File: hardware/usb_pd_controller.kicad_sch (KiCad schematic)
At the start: 87 parts, among them J4 SolderWire-1.5sqmm, J5 Banana_4mm_Red, J6 Banana_4mm_Black, Q1 BSS138, Q2 BSS138, Q3 SQJB60EP, Q5 SQJB60EP, U1 AP33772SDKZ-13-FA02, U11 TPS55340PWPR, U12 LM74801-Q1, U13 74LVC1G08, U3 INA226, U5 AOZ1284PI, U6 TL431AIDBZR

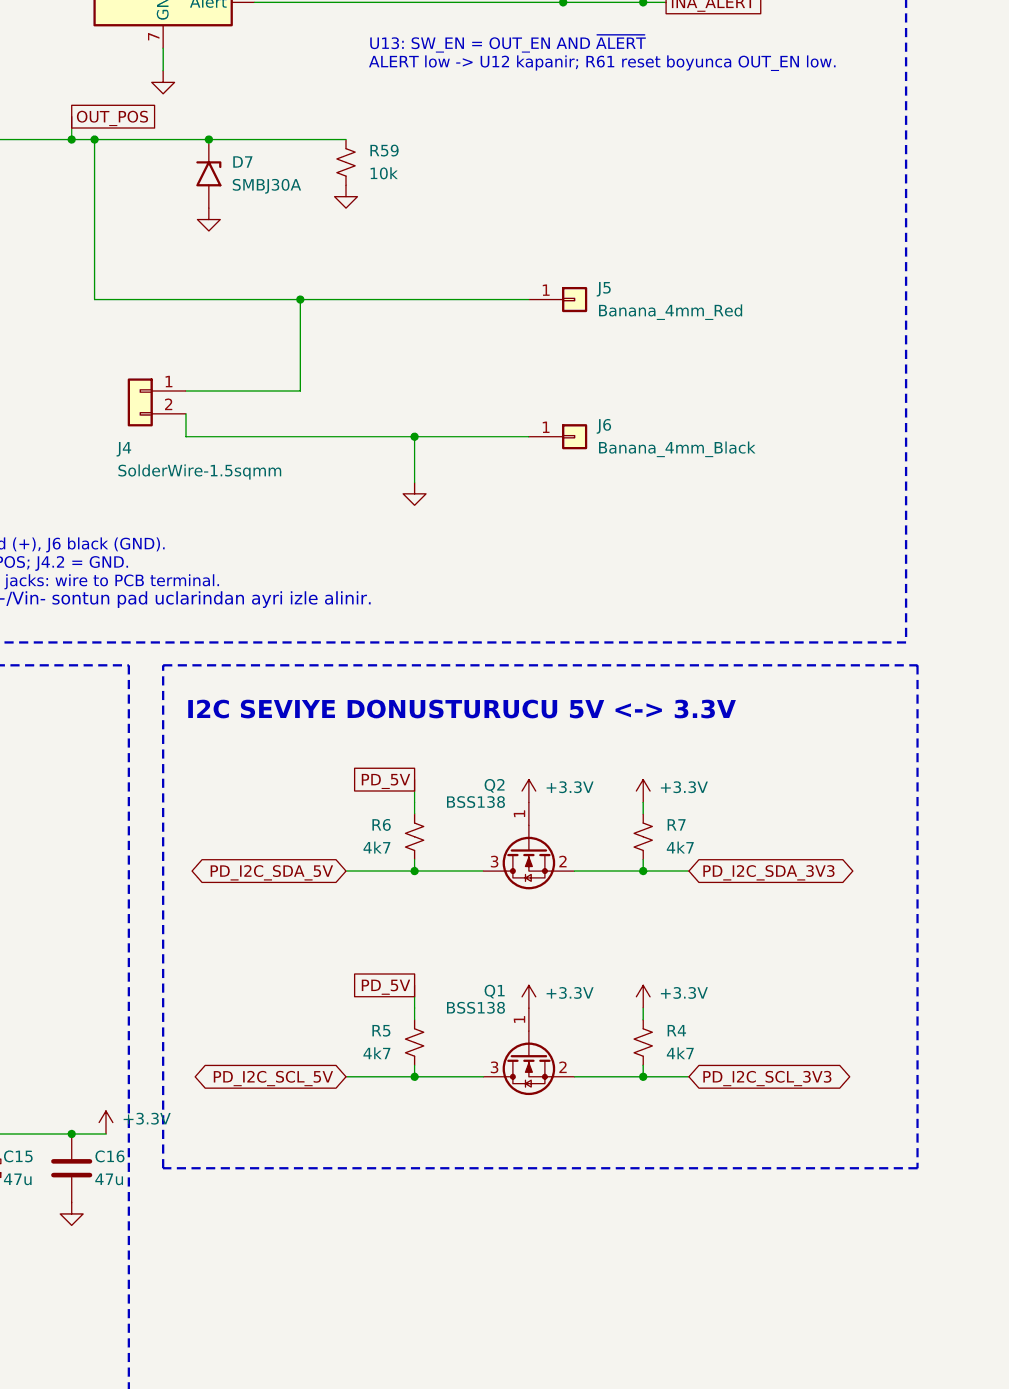
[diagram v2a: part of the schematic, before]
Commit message: hardware: I2C seviye dönüştürücüyü mcu'ya taşı, OUT_POS aktif deşarjı ekle (TASK-048/049/050)
- mcu: I2C seviye dönüştürücü (Q1, Q2, R4-R7) usb_pd_controller'dan
  taşındı; sayfa A4 -> A3. Bağlantı değişmedi.
- usb_pd_controller: R59 bleed yerine SW_EN kontrollü deşarj. Q4 BSS138P
  SW_EN'i ters çevirir, Q6 BSS138P OUT_POS'u R67 1k 2W 2512 üzerinden
  boşaltır; gate SW_OUT'tan R66 100k, D10 BZT52C12 ile 12 V. R59 10k 0805
  -> 100k 0603. Q1/Q2 alanları BSS138P,215 datasheet'ine göre düzeltildi.
- Karar: design_decisions/output/CIKIS_DESARJI_20260923.md; firmware
  deşarj bekleme ve dış kaynak uyarısı FIRMWARE_GEREKSINIMLERI.md §3.
- Backlog: TASK-048/049 Done, TASK-050 bring-up doğrulaması açıldı,
  TASK-006'ya footprint notu.

Kanıt: ERC 0/0. Netlist farkı yalnız beklenen netler: yeni DISCH_G
(D10.1, Q4.3, Q6.1, R66.2) ve Net-(Q6-D) (Q6.3, R67.2); SW_EN += Q4.1,
SW_OUT += R66.1, OUT_POS += R67.1, GND += D10.2, Q4.2, Q6.2.

Co-Authored-By: Claude Opus 5.5 <noreply@anthropic.com>
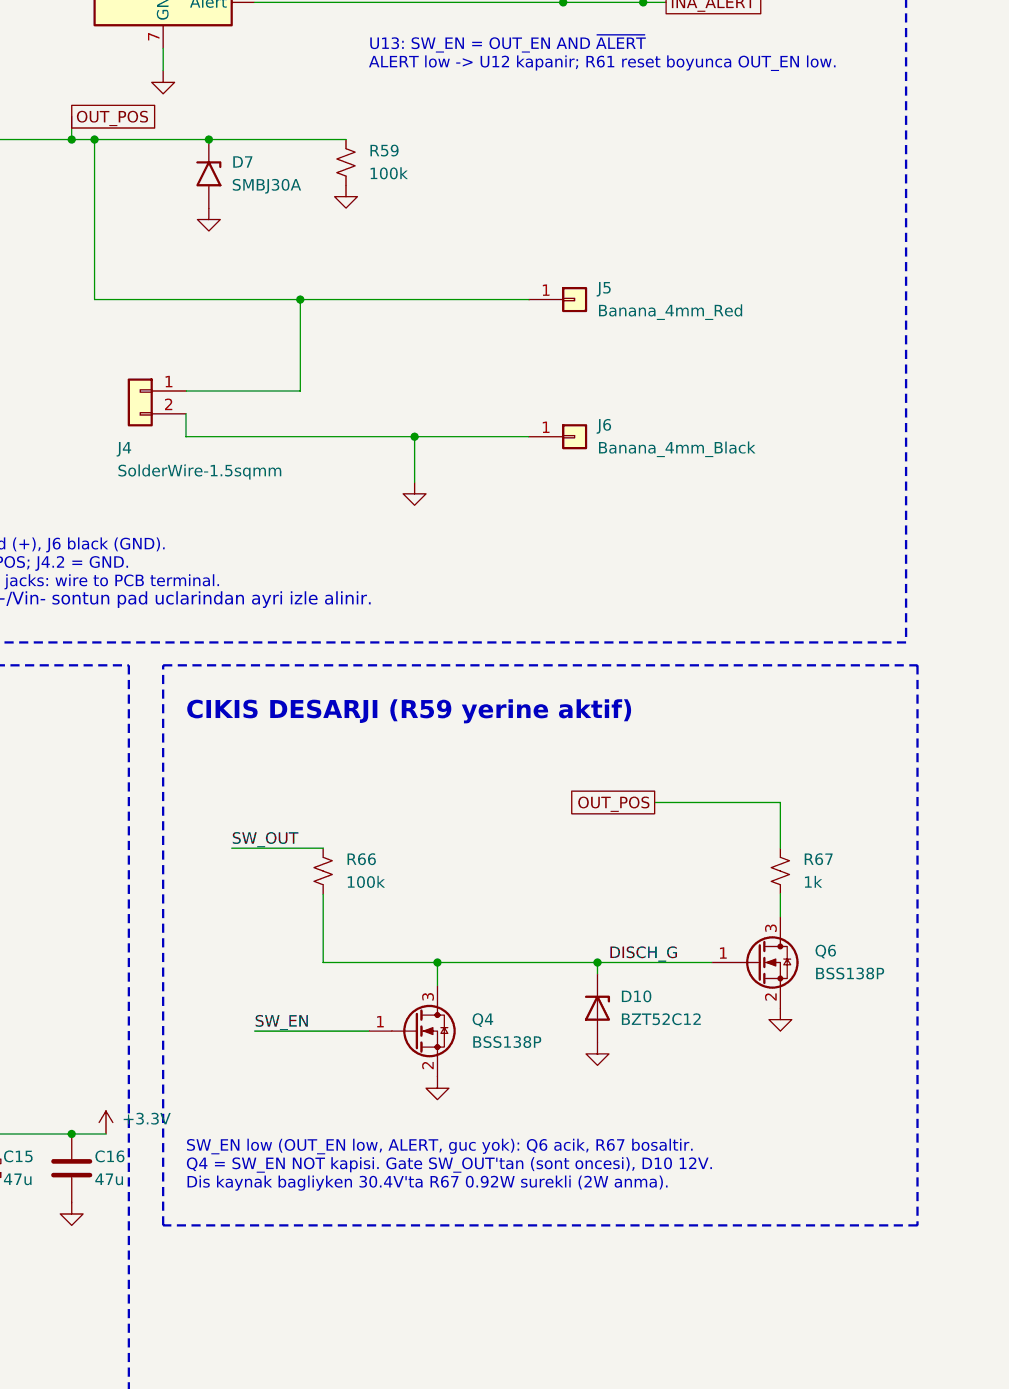
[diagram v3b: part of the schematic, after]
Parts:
- removed Q1, Q2: BSS138, Package_TO_SOT_SMD:SOT-23, symbol Transistor_FET:BSS138
- removed R4, R5, R6, R7: 4k7, Resistor_SMD:R_0402_1005Metric, symbol Device:R_Small_US
- added D10: BZT52C12, Diode_SMD:D_SOD-123, symbol Device:D_Zener
- added Q4, Q6: BSS138P, Package_TO_SOT_SMD:SOT-23, symbol Transistor_FET:BSS138
- added R66: 100k, Resistor_SMD:R_0603_1608Metric, symbol Device:R_Small_US
- added R67: 1k, Resistor_SMD:R_2512_6332Metric, symbol Device:R_Small_US
- R59: value 10k -> 100k; footprint Resistor_SMD:R_0805_2012Metric -> Resistor_SMD:R_0603_1608Metric; Composition High Power Thick Film -> Thick Film; DesignNote OUT_POS bleed. 30V OVLO esiginde 90mW; %50 azaltma ile >=0.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 -> OUT_POS son bleed: Q6 eşiği (~1.5V) altını boşaltır, INA226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; MPN HP05W3F1002T5E -> CRCW0603100KFKTBBC; Manufacturer Royalohm -> Vishay; Package 0805 (2012 Metric) -> 0603 (1608 Metric); PowerRating 0.333W -> 0.1W; SelectionNote Özdisan 604238; stok 710 (21.09.2026); Uygun. 21.09 üçüncü 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 -> Özdisan 1089735; stok 8494 (23.09.2026); Uygun.; VoltageRating 150V -> 75V
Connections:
- net GND: now also D10.2 (A), Q4.2 (S), Q6.2 (S)
- net OUT_POS: now also R67.1
- net SW_EN: now also Q4.1 (G)
- net SW_OUT: now also R66.1
- new net: Q6.3 (D), R67.2
- new net DISCH_G: D10.1 (K), Q4.3 (D), Q6.1 (G), R66.2
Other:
- note added: "CIKIS DESARJI (R59 yerine aktif)"
- note added: "SW_EN low (OUT_EN low, ALERT, guc yok): Q6 acik, R67 bosaltir. Q4 = SW_EN NOT kapisi. Gate SW_OUT'tan (sont oncesi), D10 12V. Dis kaynak bagliyken 30.4V'ta R67 0.92W surekli (2W anma)."
- note removed: "I2C SEVIYE DONUSTURUCU 5V <-> 3.3V"

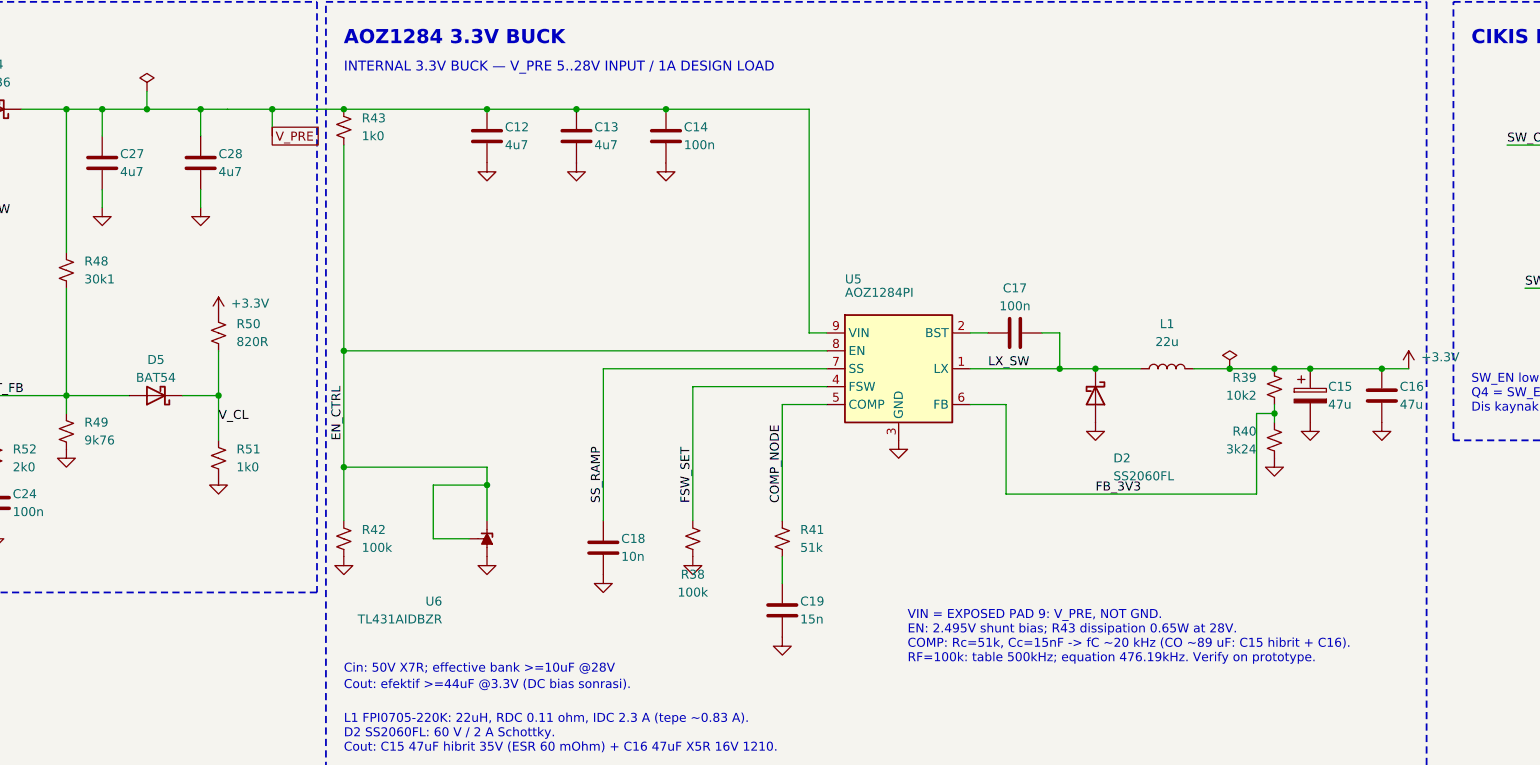
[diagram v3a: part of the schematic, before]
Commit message: hardware: U5 EN ve U11 FB clamp icin ortak V_X referansi (TASK-057)
FB clamp referansi (V_CL) +3.3V'tan besleniyordu; +3.3V ise V_PRE'den
uretildigi icin acilista ve 3V3 kaybinda clamp FB'yi asagi cekiyordu.
EN_CTRL ve clamp tek TLV431 dugumunde birlesti: V_X = 1.605 V.

- U6 TL431AIDBZR -> TLV431BQDBZT; yeni proje sembolu
  Power_Path_Custom:TLV431xDBZ (DBZ: 1=REF, 2=K, 3=A, SLVS139Z Tablo 4-1)
- R50 2k87 / R51 9k76 U6 REF bolucusu oldu, U6 yanina tasindi
- D5 BAT54 (SOD-123) -> BAS16HT1G (SOD-323), katot EN_CTRL'de
- R43 1k0 2W -> 4k7 1W (28 V'ta 0.65 W -> 0.15 W), R42 kaldirildi

Worst-case (0-60 C, V_PRE 4.3-34 V): FB <= 2.40 V (abs 3 V), EN
1.566-1.652 V, U6 akimi 0.41-7.8 mA. ERC 0/0; netlist farki yalniz
EN_CTRL, yeni Net-(U6-REF), V_CL kalkti, +3.3V/GND'den R50/R42 cikti.
PCB guncellemesi TASK-058, olcum TASK-059.

Co-Authored-By: Claude Opus 5.5 <noreply@anthropic.com>
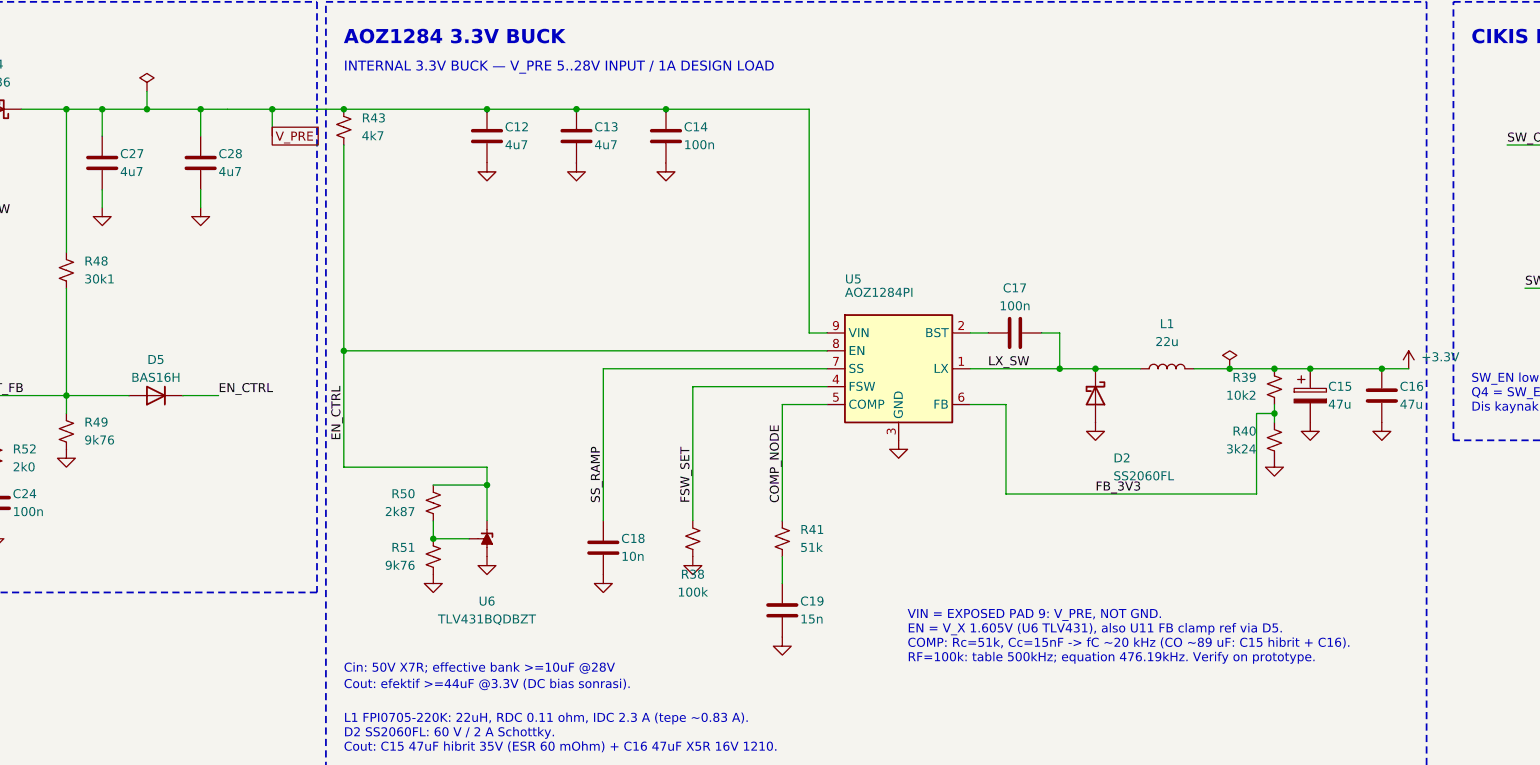
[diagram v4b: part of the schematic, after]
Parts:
- removed R42: 100k, Resistor_SMD:R_0402_1005Metric, symbol Device:R_Small_US
- D5: value BAT54 -> BAS16H; footprint Diode_SMD:D_SOD-123 -> Diode_SMD:D_SOD-323; symbol Device:D_Schottky -> Device:D; DesignNote TBD -> Si diyot: Schottky kacagi FB ofsetine girmesin. FB worst 2.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; DiodeType Schottky -> Switching; ForwardCurrent TBD -> 200mA; ForwardVoltage TBD -> 715mV @1mA; MPN BAT54T1G -> BAS16HT1G; Package SOD-123 -> SOD-323; ReverseCurrent TBD -> 1uA @100V; ReverseVoltage TBD -> 100V; SelectionNote Özdisan 614028; stok 595 (21.09.2026); Uygun. Otomatik MPN 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 -> Özdisan 344295; stok 6290 (23.09.2026); Uygun.
- R43: value 1k0 -> 4k7; Composition Anti-Surge Thick Film -> Thick Film; DesignNote Sont besleme: 28V'ta 0.651W. Gercek 2W parca secilecek; aya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 -> V_X besleme: 29.4V surekli 0.17W, 34V gecici 0.23W.; MPN PS122WF1001T4E -> CQ121WF4701T4E; PowerRating 2W -> 1W; SelectionNote Özdisan 746122; stok 93571 (21.09.2026); Uygun. 2W şartı (2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 -> Özdisan 605074; stok 10274 (23.09.2026); Uygun. AEC-Q200 %1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; VoltageRating 500V -> 200V
- R50: value 820R -> 2k87; DesignNote TBD -> U6 REF bolucu ust (EN_CTRL -> REF).; MPN RC0402JR-07820RL -> 0402WGF2871TCE; Manufacturer Yageo -> Royalohm; SelectionNote Özdisan 423409; stok 92000 (21.09.2026); Uygun. 0402 820R y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 -> Özdisan 506262; stok 7770 (23.09.2026); Uygun. R48/R49 ile 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; Tolerance +/-5% -> +/-1%
- R51: value 1k0 -> 9k76; Composition Thin Film -> Thick Film; DesignNote TBD -> U6 REF bolucu alt (REF -> GND).; MPN RT0402BRD071KL -> 0402WGF9761TCE; Manufacturer Yageo -> Royalohm; SelectionNote Özdisan 1212342; stok 37995 (21.09.2026); Uygun. 0402 1k %1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 -> Özdisan 506310; stok 17170 (23.09.2026); Uygun. R49 ile ayn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; TempCoefficient +/-25ppm/C -> +/-100ppm/C; Tolerance +/-0.1% -> +/-1%
- U6: value TL431AIDBZR -> TLV431BQDBZT; symbol Reference_Voltage:TL431DBZ -> Power_Path_Custom:TLV431xDBZ; DesignNote TI TL431 DBZ: K=1, REF=2, A=3. REF, K'ya bagli. Ek kapasiti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 -> TLV431 DBZ: REF=1, K=2, A=3 (TI SLVS139Z Table 4-1). V_X he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; MPN TL431AIDBZR -> TLV431BQDBZT; OperatingTemp TBD -> -40C..125C; PinCount TBD -> 3; SelectionNote Özdisan 341981; stok 2428 (21.09.2026); Muadil. B sınıfı (%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 -> Özdisan 1587549; stok 1134 (23.09.2026); Uygun. B sınıfı %0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; Subcategory Linear - Amplifiers / Data Acquisition -> PMIC - Voltage Reference; SupplyVoltage TBD -> VKA 1.24..6V
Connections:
- net +3.3V: no longer R50.1
- net EN_CTRL: now also D5.1 (K), R50.1; no longer U6.1 (K)
- net V_CL: no longer names the net of R50.2, R51.1
- net V_CL: now also U6.1 (REF); no longer D5.1 (K)
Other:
- note added: "VIN = EXPOSED PAD 9: V_PRE, NOT GND. EN = V_X 1.605V (U6 TLV431), also U11 FB clamp ref via D5. COMP: Rc=51k, Cc=15nF -> fC ~20 kHz (CO ~89 uF: C15 hibrit + C16). RF=100k: table 500kHz; equation 476.19kHz. Verify on prototype."
- note removed: "VIN = EXPOSED PAD 9: V_PRE, NOT GND. EN: 2.495V shunt bias; R43 dissipation 0.65W at 28V. COMP: Rc=51k, Cc=15nF -> fC ~20 kHz (CO ~89 uF: C15 hibrit + C16). RF=100k: table 500kHz; equation 476.19kHz. Verify on prototype."
- moved on the sheet: R50, R51
